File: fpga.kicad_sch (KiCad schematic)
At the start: 68 parts, among them U9 LIFCL-40-9BG256C

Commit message: Added indicator LEDs and user switch
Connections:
- net LED0: now reaches U9.E15 (PT84A)
- net LED1: now reaches U9.E16 (PT84B)
- net DIP4: now reaches U9.H10 (PR30B)
- net DIP3: now reaches U9.H11 (PR30A/PCLKT2_0)
- net DIP5: now reaches U9.H13 (PR32A/PCLKT2_1)
- net DIP2: now reaches U9.H14 (PR27B)
- net DIP1: now reaches U9.H15 (PR27A)
- net DIP0: now reaches U9.H16 (PR26A)
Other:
- moved on the sheet: C?, R?, TP?, U?

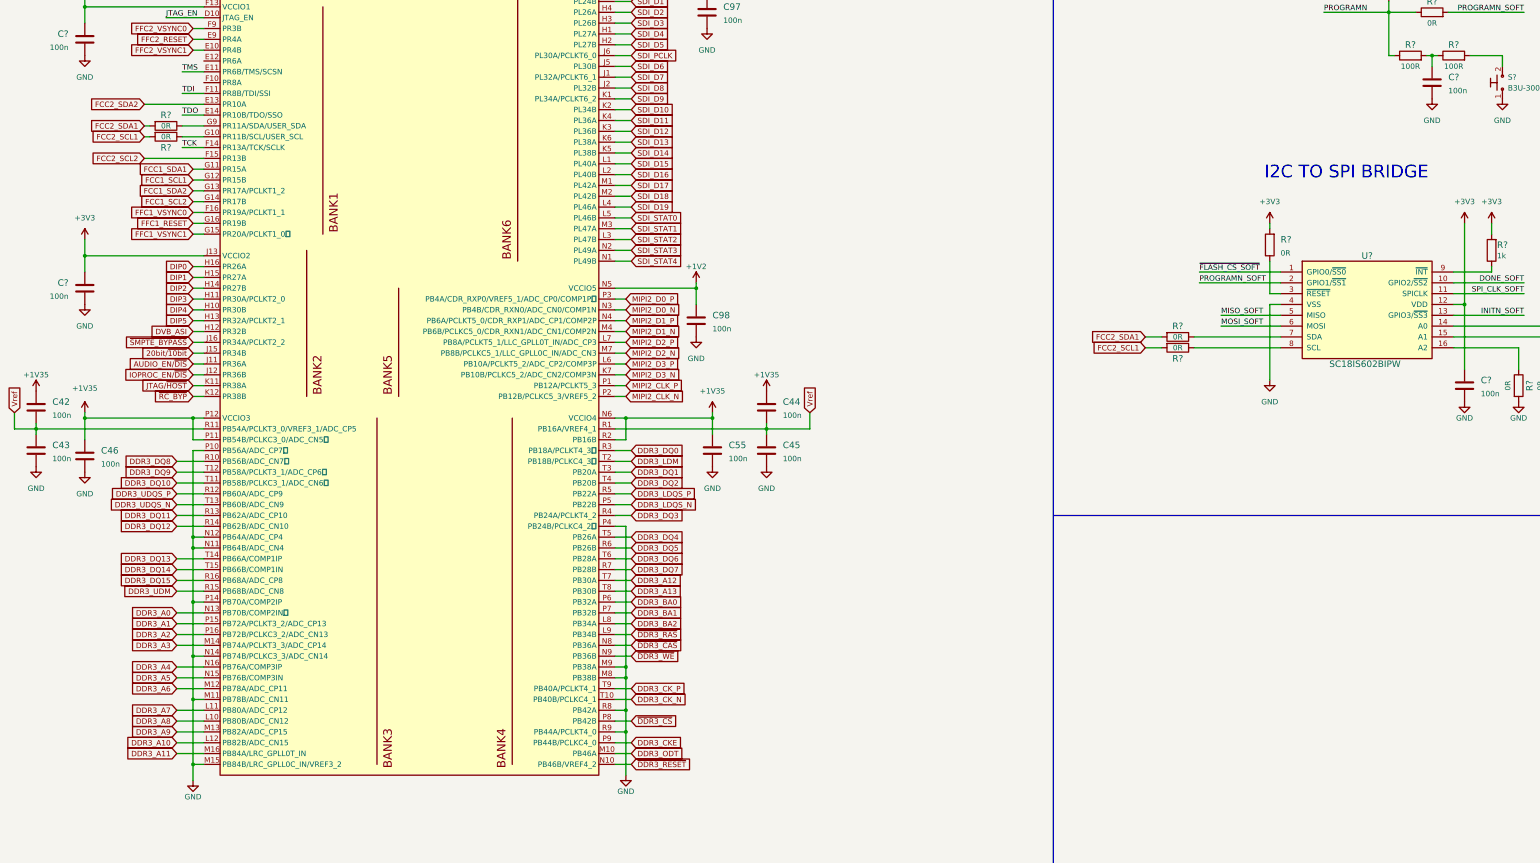
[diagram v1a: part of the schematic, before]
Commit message: Added optional oscillator
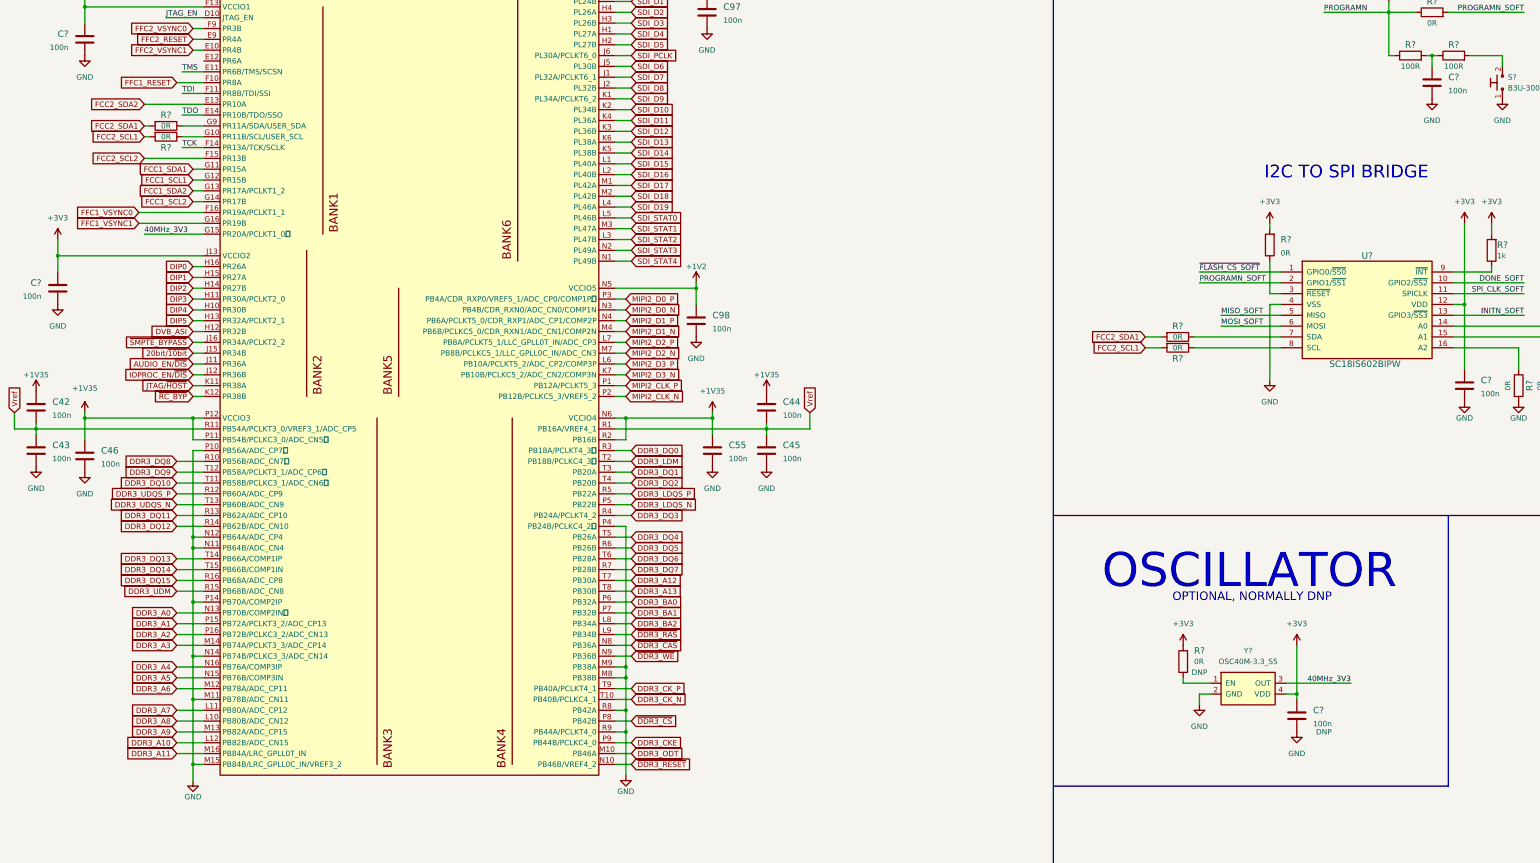
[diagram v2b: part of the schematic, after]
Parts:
- added C?: C_100n_0603, antmicro-footprints:0603-cap, symbol antmicroCapacitors0603:C_100n_0603
- added R?: R_0R_0603, antmicro-footprints:0603-res, symbol antmicroResistors0603:R_0R_0603
- added Y?: OSC40M-3.3_S5, antmicro-footprints:OSC-4_5.0x3.2mm, symbol antmicroOscillators:OSC40M-3.3_S5
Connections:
- net +3V3: now also C?.1, R?.2, Y?.4 (VDD)
- net FFC1_RESET: now also U9.F10 (PR8A); no longer U9.G16 (PR19B)
- net FFC1_VSYNC1: now also U9.G16 (PR19B); no longer U9.G15 (PR20A/PCLKT1_0 )
- net GND: now also C?.2, Y?.2 (GND)
- new net: R?.1, Y?.1 (EN)
- new net 40MHz_3V3: U9.G15 (PR20A/PCLKT1_0 ), Y?.3 (OUT)
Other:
- note added: "OPTIONAL, NORMALLY DNP"
- note added: "OSCILLATOR"
- moved on the sheet: C?

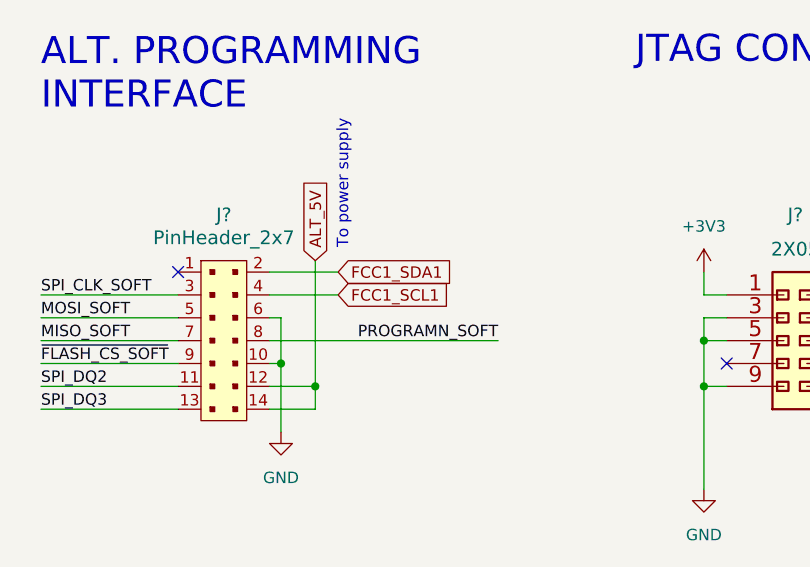
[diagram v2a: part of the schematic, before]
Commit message: Small I2C connection fix
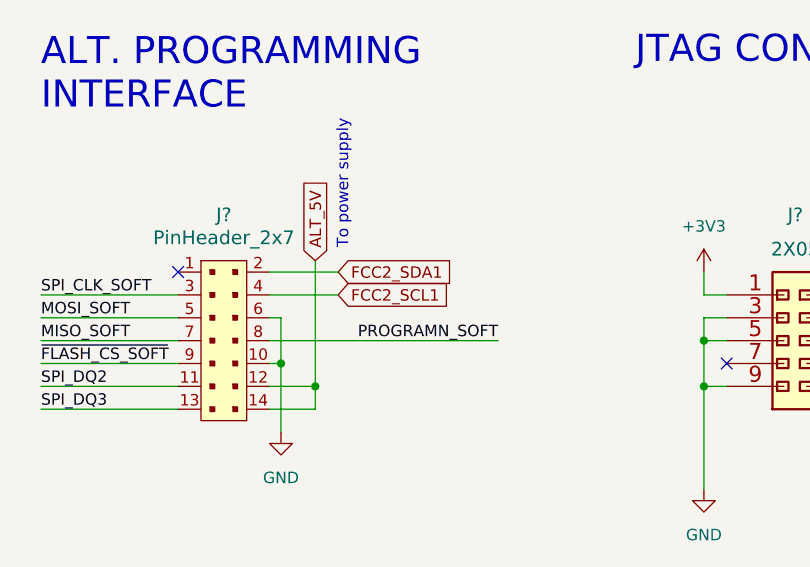
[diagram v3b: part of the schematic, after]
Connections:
- net FCC1_SCL1: no longer J?.4
- net FCC1_SDA1: no longer J?.2
- net FCC2_SCL1: now also J?.4
- net FCC2_SDA1: now also J?.2
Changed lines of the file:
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@@
     )
   )
-  (global_label "FCC1_SCL1" (shape input) (at 481.33 232.41 0) (fields_autoplaced)
+  (global_label "FCC2_SCL1" (shape input) (at 481.33 232.41 0) (fields_autoplaced)
     (effects (font (size 1.27 1.27)) (justify left))
     (property "Intersheet References" "${INTERSHEET_REFS}" (id 0) (at 494.266 232.3306 0)
@@
     )
   )
-  (global_label "FCC1_SDA1" (shape input) (at 481.33 229.87 0) (fields_autoplaced)
+  (global_label "FCC2_SDA1" (shape input) (at 481.33 229.87 0) (fields_autoplaced)
     (effects (font (size 1.27 1.27)) (justify left))
     (property "Intersheet References" "${INTERSHEET_REFS}" (id 0) (at 494.3264 229.7906 0)

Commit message: Made PCB mockup
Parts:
- removed J?: PinHeader_2x7, antmicro-footprints:PinHeader_2x07_P2.54mm_Vertical, symbol antmicroRectangularConnectorsHeadersMalePins:PinHeader_2x7
- removed U9: LIFCL-40-9BG256C, antmicro-footprints:BGA-256_16x16_14.0x14.0mm, symbol antmicroBGAchips:LIFCL-40-9BG256C
- added J7: FTSH-105-01-L-DV-K, antmicro-footprints:PinHeader_2x5_P1.27_SMD, symbol antmicroRectangularConnectorsHeadersMalePins:FTSH-105-01-L-DV-K
- added U11: LIFCL-40-9BG256C, antmicro-footprints:BGA-256_16x16_14.0x14.0mm, symbol antmicroBGAchips:LIFCL-40-9BG256C
- gave numbers to parts that had none: 60
- renumbered C42 to C68, C43 to C69, C46 to C73, C96 to C74, C98 to C75, C97 to C76, C55 to C77, C44 to C78, C45 to C79
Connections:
- net +1V2: now also U11.N5 (VCCIO5)
- net +1V35: now also U11.N6 (VCCIO4), U11.P11 (PB54B/PCLKC3_0/ADC_CN5 ), U11.P12 (VCCIO3), U11.R2 (PB16B)
- net +3V3: now also U11.D13 (VCCIO0), U11.F13 (VCCIO1), U11.F5 (VCCIO7), U11.J13 (VCCIO2), U11.J4 (VCCIO6)
- net 20bit/~{10bit}: now also U11.J15 (PR34B)
- net 40MHz_3V3: now also U11.G15 (PR20A/PCLKT1_0 )
- net AUDIO_EN/~{DIS}: now also U11.J11 (PR36A)
- net DDR3_A0: now also U11.N13 (PB70B/COMP2IN )
- net DDR3_A1: now also U11.P15 (PB72A/PCLKT3_2/ADC_CP13)
- net DDR3_A10: now also U11.L12 (PB82B/ADC_CN15)
- net DDR3_A11: now also U11.M16 (PB84A/LRC_GPLL0T_IN)
- net DDR3_A12: now also U11.T7 (PB30A)
- net DDR3_A13: now also U11.T8 (PB30B)
- net DDR3_A2: now also U11.P16 (PB72B/PCLKC3_2/ADC_CN13)
- net DDR3_A3: now also U11.M14 (PB74A/PCLKT3_3/ADC_CP14)
- net DDR3_A4: now also U11.N16 (PB76A/COMP3IP)
- net DDR3_A5: now also U11.N15 (PB76B/COMP3IN)
- net DDR3_A6: now also U11.M12 (PB78A/ADC_CP11)
- net DDR3_A7: now also U11.L11 (PB80A/ADC_CP12)
- net DDR3_A8: now also U11.L10 (PB80B/ADC_CN12)
- net DDR3_A9: now also U11.M13 (PB82A/ADC_CP15)
- net DDR3_BA0: now also U11.P6 (PB32A)
- net DDR3_BA1: now also U11.P7 (PB32B)
- net DDR3_BA2: now also U11.L8 (PB34A)
- net DDR3_CKE: now also U11.P9 (PB44B/PCLKC4_0)
- net DDR3_CK_N: now also U11.T10 (PB40B/PCLKC4_1)
- net DDR3_CK_P: now also U11.T9 (PB40A/PCLKT4_1)
- net DDR3_DQ0: now also U11.R3 (PB18A/PCLKT4_3 )
- net DDR3_DQ1: now also U11.T3 (PB20A)
- net DDR3_DQ10: now also U11.T11 (PB58B/PCLKC3_1/ADC_CN6 )
- net DDR3_DQ11: now also U11.R13 (PB62A/ADC_CP10)
- net DDR3_DQ12: now also U11.R14 (PB62B/ADC_CN10)
- net DDR3_DQ13: now also U11.T14 (PB66A/COMP1IP)
- net DDR3_DQ14: now also U11.T15 (PB66B/COMP1IN)
- net DDR3_DQ15: now also U11.R16 (PB68A/ADC_CP8)
- net DDR3_DQ2: now also U11.T4 (PB20B)
- net DDR3_DQ3: now also U11.R4 (PB24A/PCLKT4_2)
- net DDR3_DQ4: now also U11.T5 (PB26A)
- net DDR3_DQ5: now also U11.R6 (PB26B)
- net DDR3_DQ6: now also U11.T6 (PB28A)
- net DDR3_DQ7: now also U11.R7 (PB28B)
- net DDR3_DQ8: now also U11.R10 (PB56B/ADC_CN7 )
- net DDR3_DQ9: now also U11.T12 (PB58A/PCLKT3_1/ADC_CP6 )
- net DDR3_LDM: now also U11.T2 (PB18B/PCLKC4_3 )
- net DDR3_LDQS_N: now also U11.P5 (PB22B)
- net DDR3_LDQS_P: now also U11.R5 (PB22A)
- net DDR3_ODT: now also U11.M10 (PB46A)
- net DDR3_UDM: now also U11.R15 (PB68B/ADC_CN8)
- net DDR3_UDQS_N: now also U11.T13 (PB60B/ADC_CN9)
- net DDR3_UDQS_P: now also U11.R12 (PB60A/ADC_CP9)
- net DIP0: now also U11.H16 (PR26A)
- net DIP1: now also U11.H15 (PR27A)
- net DIP2: now also U11.H14 (PR27B)
- net DIP3: now also U11.H11 (PR30A/PCLKT2_0)
- net DIP4: now also U11.H10 (PR30B)
- net DIP5: now also U11.H13 (PR32A/PCLKT2_1)
- net DONE: now also U11.B16 (PT76B/DONE )
- net DVB_ASI: now also U11.H12 (PR32B)
- net FCC1_SCL1: now also U11.G12 (PR15B)
- net FCC1_SCL2: now also U11.G14 (PR17B)
- net FCC1_SDA1: now also U11.G11 (PR15A)
- net FCC1_SDA2: now also U11.G13 (PR17A/PCLKT1_2)
- net FCC2_SCL1: now also J7.4
- net FCC2_SCL2: now also U11.F15 (PR13B)
- net FCC2_SDA1: now also J7.2
- net FCC2_SDA2: now also U11.E13 (PR10A)
- net FFC1_RESET: now also U11.F10 (PR8A)
- net FFC1_VSYNC0: now also U11.F16 (PR19A/PCLKT1_1)
- net FFC1_VSYNC1: now also U11.G16 (PR19B)
- net FFC2_RESET: now also U11.E9 (PR4A)
- net FFC2_VSYNC0: now also U11.F9 (PR3B)
- net FFC2_VSYNC1: now also U11.E10 (PR4B)
- net GND: now also J7.10, J7.6, U11.M11 (PB78B/ADC_CN11), U11.M15 (PB84B/LRC_GPLL0C_IN/VREF3_2), U11.M8 (PB38B), U11.M9 (PB38A), U11.N11 (PB64B/ADC_CN4), U11.N12 (PB64A/ADC_CP4), U11.N14 (PB74B/PCLKC3_3/ADC_CN14), U11.P10 (PB56A/ADC_CP7 ), U11.P14 (PB70A/COMP2IP), U11.P4 (PB24B/PCLKC4_2 ), U11.R8 (PB42A), U11.R9 (PB44A/PCLKT4_0)
- net INITN: now also U11.D11 (PT74A/INITN )
- net IOPROC_EN/~{DIS}: now also U11.J12 (PR36B)
- net JTAG_EN: now also U11.D10 (JTAG_EN)
- net JTAG/~{HOST}: now also U11.K11 (PR38A)
- net LED0: now also U11.E15 (PT84A)
- net LED1: now also U11.E16 (PT84B)
- net MIPI0_CLK_N: now also U11.D2 (DPHY0_CKN)
- net MIPI0_CLK_P: now also U11.D1 (DPHY0_CKP)
- net MIPI0_D0_N: now also U11.E2 (DPHY0_DN0)
- net MIPI0_D0_P: now also U11.E1 (DPHY0_DP0)
- net MIPI0_D1_N: now also U11.C2 (DPHY0_DN1)
- net MIPI0_D1_P: now also U11.C1 (DPHY0_DP1)
- net MIPI0_D2_N: now also U11.F2 (DPHY0_DN2)
- net MIPI0_D2_P: now also U11.F1 (DPHY0_DP2)
- net MIPI0_D3_N: now also U11.B2 (DPHY0_DN3)
- net MIPI0_D3_P: now also U11.B1 (DPHY0_DP3)
- net MIPI1_CLK_N: now also U11.B5 (DPHY1_CKN)
- net MIPI1_CLK_P: now also U11.A5 (DPHY1_CKP)
- net MIPI1_D0_N: now also U11.B4 (DPHY1_DN0)
- net MIPI1_D0_P: now also U11.A4 (DPHY1_DP0)
- net MIPI1_D1_N: now also U11.B6 (DPHY1_DN1)
- net MIPI1_D1_P: now also U11.A6 (DPHY1_DP1)
- net MIPI1_D2_N: now also U11.B3 (DPHY1_DN2)
- net MIPI1_D2_P: now also U11.A3 (DPHY1_DP2)
- net MIPI1_D3_N: now also U11.B7 (DPHY1_DN3)
- net MIPI1_D3_P: now also U11.A7 (DPHY1_DP3)
- net MIPI2_CLK_N: now also U11.P2 (PB12B/PCLKC5_3/VREF5_2)
- net MIPI2_CLK_P: now also U11.P1 (PB12A/PCLKT5_3)
- net MIPI2_D0_N: now also U11.N3 (PB4B/CDR_RXN0/ADC_CN0/COMP1N)
- net MIPI2_D0_P: now also U11.P3 (PB4A/CDR_RXP0/VREF5_1/ADC_CP0/COMP1P )
- net MIPI2_D1_N: now also U11.M4 (PB6B/PCLKC5_0/CDR_RXN1/ADC_CN1/COMP2N)
- net MIPI2_D1_P: now also U11.N4 (PB6A/PCLKT5_0/CDR_RXP1/ADC_CP1/COMP2P)
- net MIPI2_D2_N: now also U11.M7 (PB8B/PCLKC5_1/LLC_GPLL0C_IN/ADC_CN3)
- net MIPI2_D2_P: now also U11.L7 (PB8A/PCLKT5_1/LLC_GPLL0T_IN/ADC_CP3)
- net MIPI2_D3_N: now also U11.K7 (PB10B/PCLKC5_2/ADC_CN2/COMP3N)
- net MIPI2_D3_P: now also U11.L6 (PB10A/PCLKT5_2/ADC_CP2/COMP3P)
- net MISO_SOFT: now also J7.7
- net MOSI_SOFT: now also J7.5
- net PROGRAMN: now also U11.C12 (PT74B/PROGRAMN)
- net PROGRAMN_SOFT: now also J7.8
- net RESET_TRST: now also U11.D4 (PL3A/ULC_GPLL0T_IN)
- net SCLK_TCK: now also U11.E5 (PL6B)
- net SDIN_TDI: now also U11.F6 (PL17A/PCLKT7_2)
- net SDI_D0: now also U11.H6 (PL24A)
- net SDI_D1: now also U11.H5 (PL24B)
- net SDI_D10: now also U11.K2 (PL34B)
- net SDI_D11: now also U11.K4 (PL36A)
- net SDI_D12: now also U11.K3 (PL36B)
- net SDI_D13: now also U11.K6 (PL38A)
- net SDI_D14: now also U11.K5 (PL38B)
- net SDI_D15: now also U11.L1 (PL40A)
- net SDI_D16: now also U11.L2 (PL40B)
- net SDI_D17: now also U11.M1 (PL42A)
- net SDI_D18: now also U11.M2 (PL42B)
- net SDI_D19: now also U11.L4 (PL46A)
- net SDI_D2: now also U11.H4 (PL26A)
- net SDI_D3: now also U11.H3 (PL26B)
- net SDI_D4: now also U11.H1 (PL27A)
- net SDI_D5: now also U11.H2 (PL27B)
- net SDI_D6: now also U11.J5 (PL30B)
- net SDI_D7: now also U11.J1 (PL32A/PCLKT6_1)
- net SDI_D8: now also U11.J2 (PL32B)
- net SDI_D9: now also U11.K1 (PL34A/PCLKT6_2)
- net SDI_PCLK: now also U11.J6 (PL30A/PCLKT6_0)
- net SDI_STAT0: now also U11.L5 (PL46B)
- net SDI_STAT1: now also U11.M3 (PL47A)
- net SDI_STAT2: now also U11.L3 (PL47B)
- net SDI_STAT3: now also U11.N2 (PL49A)
- net SDI_STAT4: now also U11.N1 (PL49B)
- net SDI_STAT5: now also U11.G3 (PL20A/PCLKT7_0)
- net SDOUT_TDO: now also U11.F4 (PL19A/PCLKT7_1)
- net SDO_EN/DIS: now also U11.G6 (PL17B)
- net SPI_CLK: now also U11.C16 (PT76A/MCLK/PCLKT0_0)
- net SPI_CLK_SOFT: now also J7.3
- net SPI_DQ0_MOSI: now also U11.C14 (PT78B/MOSI/MD0)
- net SPI_DQ1_MISO: now also U11.D16 (PT80A/MISO/MD1)
- net SPI_DQ2: now also U11.D15 (PT80B/MD2)
- net SPI_DQ3: now also U11.D12 (PT82A/MD3)
- net STANDBY: now also U11.D5 (PL3B/ULC_GPLL0C_IN)
- net SW_EN: now also U11.D6 (PL4A)
- net TCK: now also U11.F14 (PR13A/TCK/SCLK)
- net TDI: now also U11.F11 (PR8B/TDI/SSI)
- net TDO: now also U11.E14 (PR10B/TDO/SSO)
- net TIM_861: now also U11.E6 (PL4B)
- net TMS: now also U11.E11 (PR6B/TMS/SCSN)
- net Vref: now also U11.R1 (PB16A/VREF4_1), U11.R11 (PB54A/PCLKT3_0/VREF3_1/ADC_CP5)
- net ~{CS_TMS}: now also U11.E4 (PL6A)
- net ~{DDR3_CAS}: now also U11.N8 (PB36A)
- net ~{DDR3_CS}: now also U11.P8 (PB42B)
- net ~{DDR3_RAS}: now also U11.L9 (PB34B)
- net ~{DDR3_RESET}: now also U11.N10 (PB46B/VREF4_2)
- net ~{DDR3_WE}: now also U11.N9 (PB36B)
- net ~{FLASH_CS_SOFT}: now also J7.9
- net ~{FLASH_CS}: now also U11.C15 (PT78A/MCSN/PCLKT0_1)
- net ~{RC_BYP}: now also U11.K12 (PR38B)
- net ~{SDO_DISABLE}: now also U11.G4 (PL19B)
- net ~{SMPTE_BYPASS}: now also U11.J16 (PR34A/PCLKT2_2)
- net at R70.1: now also U11.G10 (PR11B/SCL/USER_SCL)
- net at R69.1: now also U11.G9 (PR11A/SDA/USER_SDA)

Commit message: Added loclib
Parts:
- C68, C69, C70, C71, C72, C73, C74, C75, C76, C77, C78, C79, C80, C81, C82, C83: footprint antmicro-footprints:0603-cap -> crosslink-nx-video-converter-footprints:0603-cap; symbol antmicroCapacitors0603:C_100n_0603 -> crosslink-nx-video-converter:C_100n_0603
- D11: footprint antmicro-footprints:LED_0603 -> crosslink-nx-video-converter-footprints:LED_0603; symbol antmicroLEDIndicationDiscrete:LTST-C190GKT -> crosslink-nx-video-converter:LTST-C190GKT
- D12: footprint antmicro-footprints:LED_0603 -> crosslink-nx-video-converter-footprints:LED_0603; symbol antmicroLEDIndicationDiscrete:LTST-C190KRKT -> crosslink-nx-video-converter:LTST-C190KRKT
- J7: footprint antmicro-footprints:PinHeader_2x5_P1.27_SMD -> crosslink-nx-video-converter-footprints:PinHeader_2x5_P1.27_SMD; symbol antmicroRectangularConnectorsHeadersMalePins:FTSH-105-01-L-DV-K -> crosslink-nx-video-converter:FTSH-105-01-L-DV-K
- J8: footprint antmicro-footprints:SHF-105-01-X-D-SM -> crosslink-nx-video-converter-footprints:SHF-105-01-X-D-SM; symbol antmicroRectangularConnectorsHeadersMalePins:2X05 -> crosslink-nx-video-converter:2X05
- Q13: footprint antmicro-footprints:SOT-23-3 -> crosslink-nx-video-converter-footprints:SOT-23-3; symbol antmicroTransistorsFETsMOSFETsSingle:2N7002 -> crosslink-nx-video-converter:2N7002
- R100, R101, R102, R103, R104, R69, R70, R71, R72, R73, R74, R77, R80, R81, R82, R83, R84, R85, R86, R87, R88, R89, R92, R98: footprint antmicro-footprints:0603-res -> crosslink-nx-video-converter-footprints:0603-res; symbol antmicroResistors0603:R_0R_0603 -> crosslink-nx-video-converter:R_0R_0603
- R105, R75, R91, R97: footprint antmicro-footprints:0603-res -> crosslink-nx-video-converter-footprints:0603-res; symbol antmicroResistors0603:R_10k_0603 -> crosslink-nx-video-converter:R_10k_0603
- R76, R78, R94: footprint antmicro-footprints:0603-res -> crosslink-nx-video-converter-footprints:0603-res; symbol antmicroResistors0603:R_100R_0603 -> crosslink-nx-video-converter:R_100R_0603
- R79: footprint antmicro-footprints:0603-res -> crosslink-nx-video-converter-footprints:0603-res; symbol antmicroResistors0603:R_1k_0603 -> crosslink-nx-video-converter:R_1k_0603
- R90, R93, R95: footprint antmicro-footprints:0603-res -> crosslink-nx-video-converter-footprints:0603-res; symbol antmicroResistors0603:R_4k7_0603 -> crosslink-nx-video-converter:R_4k7_0603
- R96, R99: footprint antmicro-footprints:0603-res -> crosslink-nx-video-converter-footprints:0603-res; symbol antmicroResistors0603:R_2k2_0603 -> crosslink-nx-video-converter:R_2k2_0603
- S1: footprint antmicro-footprints:B3U-3000P -> crosslink-nx-video-converter-footprints:B3U-3000P; symbol antmicroPushbuttonSwitches:B3U-3000PM -> crosslink-nx-video-converter:B3U-3000PM
- TP16, TP17, TP18, TP19, TP20, TP21, TP22, TP23: footprint antmicro-footprints:TP-R-1.5 -> crosslink-nx-video-converter-footprints:TP-R-1.5; symbol antmicroTestPoints:TP -> crosslink-nx-video-converter:TP
- U11: footprint antmicro-footprints:BGA-256_16x16_14.0x14.0mm -> crosslink-nx-video-converter-footprints:BGA-256_16x16_14.0x14.0mm; symbol antmicroBGAchips:LIFCL-40-9BG256C -> crosslink-nx-video-converter:LIFCL-40-9BG256C
- U12: footprint antmicro-footprints:SC18IS602B -> crosslink-nx-video-converter-footprints:SC18IS602B; symbol antmicroInterfaceDriversReceiversTransceivers:SC18IS602BIPW -> crosslink-nx-video-converter:SC18IS602BIPW
- U13: footprint antmicro-footprints:SOIC-8_W5.3mm -> crosslink-nx-video-converter-footprints:SOIC-8_W5.3mm; symbol antmicroMemory:W25Q32JVSSIQ -> crosslink-nx-video-converter:W25Q32JVSSIQ
- Y2: footprint antmicro-footprints:OSC-4_5.0x3.2mm -> crosslink-nx-video-converter-footprints:OSC-4_5.0x3.2mm; symbol antmicroOscillators:OSC40M-3.3_S5 -> crosslink-nx-video-converter:OSC40M-3.3_S5

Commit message: Divided FPGA into multiple blocks
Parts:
- removed C68, C69, C70, C72, C73, C74, C75, C76, C77, C78, C79: C_100n_0603, crosslink-nx-video-converter-footprints:0603-cap, symbol crosslink-nx-video-converter:C_100n_0603
- removed J7: FTSH-105-01-L-DV-K, crosslink-nx-video-converter-footprints:PinHeader_2x5_P1.27_SMD, symbol crosslink-nx-video-converter:FTSH-105-01-L-DV-K
- removed R69, R70: R_0R_0603, crosslink-nx-video-converter-footprints:0603-res, symbol crosslink-nx-video-converter:R_0R_0603
- removed U11: LIFCL-40-9BG256C, crosslink-nx-video-converter-footprints:BGA-256_16x16_14.0x14.0mm, symbol crosslink-nx-video-converter:LIFCL-40-9BG256C
- added J?: PinHeader_2x4, antmicro-footprints:PinHeader_2x04_P2.54mm_Vertical, symbol antmicroRectangularConnectorsHeadersMalePins:PinHeader_2x4
- added U? (x3): LIFCL-40-9BG256C, antmicro-footprints:BGA-256_16x16_14.0x14.0mm, symbol antmicroBGAchips:LIFCL-40-9BG256C
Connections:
- net +3V3: now also U?.D13 (VCCIO0)
- net DONE: now also U?.B16 (PT76B/DONE )
- net GND: now also J?.2, J?.4, J?.6, J?.8
- net INITN: now also U?.D11 (PT74A/INITN )
- net LED0: now also U?.E15 (PT84A)
- net LED1: now also U?.E16 (PT84B)
- net PROGRAMN: now also U?.C12 (PT74B/PROGRAMN)
- net SPI_CLK: now also U?.C16 (PT76A/MCLK/PCLKT0_0)
- net SPI_DQ0_MOSI: now also U?.C14 (PT78B/MOSI/MD0)
- net SPI_DQ1_MISO: now also U?.D16 (PT80A/MISO/MD1)
- net SPI_DQ2: now also U?.D15 (PT80B/MD2)
- net SPI_DQ3: now also U?.D12 (PT82A/MD3)
- net ~{FLASH_CS}: now also U?.C15 (PT78A/MCSN/PCLKT0_1)
- net FCC2_SCL1 renamed SCL
- net SCL: now also J?.7
- net FCC2_SDA1 renamed SDA
- net SDA: now also J?.5
- new net ALT_5V: J?.1, J?.3
- no-connect marks 4 -> 1
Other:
- note added: "I2C + ALT POWER CONNECTOR"
- note removed: "ALT. PROGRAMMING INTERFACE"
- note removed: "To power supply"
- moved on the sheet: C71, C80, C81, C82, C83, D11, D12, J8, Q13, R100, R101, R102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
